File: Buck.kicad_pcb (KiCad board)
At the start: 2 copper layers, 33.5 x 40.3 mm, 15 parts, among them J1 IN, J2 OUT, J3 Measure, U1 LT1936

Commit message: small tweaks trace layout
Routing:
- net Net-(D3-K): track 2.69 -> 4.24 mm
- net VCC: track 11.2 -> 9.96 mm
- net Id: track 36.9 -> 36.3 mm
- net Net-(R2-Pad2): track 5.30 -> 5.85 mm
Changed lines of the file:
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@@
 		(tags "capacitor handsolder")
 		(property "Reference" "C2"
-			(at 0 -1.85 0)
+			(at -3.55 -0.05 0)
 			(layer "F.SilkS")
 			(effects
@@
 		)
 	)
-	(via
-		(at 96.6 79.8)
-		(size 0.6)
-		(drill 0.3)
-		(layers "F.Cu" "B.Cu")
-		(free yes)
+	(segment
+		(start 97.7 79.8)
+		(end 98.075 79.8)
+		(width 0.25)
+		(layer "F.Cu")
 		(net 1)
 	)
+	(segment
+		(start 97.1 79.1)
+		(end 97.1 79.2)
+		(width 0.25)
+		(layer "F.Cu")
+		(net 1)
+	)
+	(segment
+		(start 97.1 79.2)
+		(end 97.7 79.8)
+		(width 0.25)
+		(layer "F.Cu")
+		(net 1)
+	)
+	(segment
+		(start 98.075 79.8)
+		(end 98.09 79.815)
+		(width 0.25)
+		(layer "F.Cu")
+		(net 1)
+	)
+	(via
+		(at 97.1 79.1)
+		(size 0.6)
+		(drill 0.3)
+		(layers "F.Cu" "B.Cu")
+		(free yes)
+		(net 1)
+	)
 	(via
 		(at 94.2 79.1)
@@
 	)
 	(segment
-		(start 94.2 79.1)
-		(end 94.9 79.8)
+		(start 97.1 79.1)
+		(end 94.2 79.1)
 		(width 0.5)
 		(layer "B.Cu")
 		(net 1)
 	)
-	(segment
-		(start 94.9 79.8)
-		(end 96.6 79.8)
-		(width 0.5)
-		(layer "B.Cu")
-		(net 1)
-	)
 	(via
 		(at 93.5 87.4)
@@
 		(net 3)
 	)
-	(via
-		(at 96.1 78.1)
-		(size 0.6)
-		(drill 0.3)
-		(layers "F.Cu" "B.Cu")
+	(segment
+		(start 103.365 81.765)
+		(end 102.39 81.765)
+		(width 0.35)
+		(layer "F.Cu")
 		(net 4)
 	)
-	(via
-		(at 103.7 82.1)
-		(size 0.6)
-		(drill 0.3)
-		(layers "F.Cu" "B.Cu")
-		(free yes)
+	(segment
+		(start 103.7 81.8)
+		(end 103.4 81.8)
+		(width 0.35)
+		(layer "F.Cu")
 		(net 4)
 	)
 	(segment
-		(start 103.7 82.1)
+		(start 103.4 81.8)
+		(end 103.365 81.765)
+		(width 0.35)
+		(layer "F.Cu")
+		(net 4)
+	)
+	(via
+		(at 98.7 77.6)
+		(size 0.6)
+		(drill 0.3)
+		(layers "F.Cu" "B.Cu")
+		(net 4)
+	)
+	(via
+		(at 103.7 81.8)
+		(size 0.6)
+		(drill 0.3)
+		(layers "F.Cu" "B.Cu")
+		(free yes)
+		(net 4)
+	)
+	(segment
+		(start 102.5 77.5)
 		(end 103.7 78.7)
 		(width 0.5)
@@
 	)
 	(segment
-		(start 103.1 78.1)
-		(end 96.1 78.1)
+		(start 103.7 78.7)
+		(end 103.7 81.8)
 		(width 0.5)
 		(layer "B.Cu")
@@
 	)
 	(segment
-		(start 103.7 78.7)
-		(end 103.1 78.1)
+		(start 98.8 77.5)
+		(end 102.5 77.5)
 		(width 0.5)
 		(layer "B.Cu")
@@
 	)
 	(segment
-		(start 92.8 104.9)
-		(end 103.1 104.9)
+		(start 98.7 77.6)
+		(end 98.8 77.5)
+		(width 0.5)
+		(layer "B.Cu")
+		(net 4)
+	)
+	(segment
+		(start 91.33 103.73)
+		(end 92.5 104.9)
 		(width 0.5)
 		(layer "B.Cu")
@@
 	)
 	(segment
+		(start 92.5 104.9)
+		(end 103.1 104.9)
+		(width 0.5)
+		(layer "B.Cu")
+		(net 5)
+	)
+	(segment
+		(start 104.5 103.5)
+		(end 104.5 101.2825)
+		(width 0.5)
+		(layer "B.Cu")
+		(net 5)
+	)
+	(segment
+		(start 91.33 103.25)
+		(end 91.33 103.73)
+		(width 0.5)
+		(layer "B.Cu")
+		(net 5)
+	)
+	(segment
 		(start 103.1 104.9)
 		(end 104.5 103.5)
-		(width 0.5)
-		(layer "B.Cu")
-		(net 5)
-	)
-	(segment
-		(start 104.5 103.5)
-		(end 104.5 101.2825)
-		(width 0.5)
-		(layer "B.Cu")
-		(net 5)
-	)
-	(segment
-		(start 91.33 103.25)
-		(end 91.33 103.43)
-		(width 0.5)
-		(layer "B.Cu")
-		(net 5)
-	)
-	(segment
-		(start 91.33 103.43)
-		(end 92.8 104.9)
 		(width 0.5)
 		(layer "B.Cu")
@@
 	)
 	(segment
-		(start 108.35 91.75)
-		(end 109.1 91.75)
-		(width 0.25)
-		(layer "F.Cu")
-		(net 7)
-	)
-	(segment
-		(start 107.4 90.8)
-		(end 108.35 91.75)
+		(start 106.95 90.8)
+		(end 109.1 90.8)
 		(width 0.25)
 		(layer "F.Cu")
@@
 	)
 	(segment
-		(start 106.95 90.8)
-		(end 107.4 90.8)
+		(start 109.1 90.8)
+		(end 109.1 91.75)
 		(width 0.25)
 		(layer "F.Cu")
@@
 	)
 	(segment
+		(start 101.8 87.8)
+		(end 103.5 86.1)
+		(width 0.5)
+		(layer "F.Cu")
+		(net 9)
+	)
+	(segment
 		(start 105.4 86.8)
 		(end 106.4 87.8)
@@
 	)
 	(segment
-		(start 104.5 86.8)
+		(start 102.9 87.3)
+		(end 102.9 86)
+		(width 0.5)
+		(layer "F.Cu")
+		(net 9)
+	)
+	(segment
+		(start 103.5 86.1)
+		(end 104.2 86.8)
+		(width 0.5)
+		(layer "F.Cu")
+		(net 9)
+	)
+	(segment
+		(start 104.2 86.8)
 		(end 105.4 86.8)
 		(width 0.5)
@@
 		(net 9)
 	)
-	(segment
-		(start 103.7 86.8)
-		(end 102.9 86)
-		(width 0.5)
-		(layer "F.Cu")
+	(via
+		(at 101.8 87.8)
+		(size 0.6)
+		(drill 0.3)
+		(layers "F.Cu" "B.Cu")
 		(net 9)
 	)
 	(segment
-		(start 104.5 86.8)
-		(end 103.7 86.8)
-		(width 0.5)
-		(layer "F.Cu")
-		(net 9)
-	)
-	(via
-		(at 104.5 86.8)
-		(size 0.6)
-		(drill 0.3)
-		(layers "F.Cu" "B.Cu")
-		(net 9)
-	)
-	(segment
-		(start 96.4 86.8)
-		(end 95.2 85.6)
+		(start 101.7 87.7)
+		(end 95.8 87.7)
 		(width 0.5)
 		(layer "B.Cu")
@@
 	)
 	(segment
-		(start 90.8 85.6)
-		(end 88.79 87.61)
+		(start 95.8 87.7)
+		(end 94.4 86.3)
 		(width 0.5)
 		(layer "B.Cu")
@@
 	)
 	(segment
-		(start 95.2 85.6)
-		(end 90.8 85.6)
+		(start 94.4 86.3)
+		(end 91.5 86.3)
 		(width 0.5)
 		(layer "B.Cu")
@@
 	)
 	(segment
-		(start 88.79 87.61)
+		(start 88.79 89.01)
 		(end 88.79 103.25)
 		(width 0.5)
@@
 	)
 	(segment
-		(start 104.5 86.8)
-		(end 96.4 86.8)
+		(start 101.8 87.8)
+		(end 101.7 87.7)
+		(width 0.5)
+		(layer "B.Cu")
+		(net 9)
+	)
+	(segment
+		(start 91.5 86.3)
+		(end 88.79 89.01)
 		(width 0.5)
 		(layer "B.Cu")
@@
 		(polygon
 			(pts
-				(xy 90.5 79.75) (xy 87.75 79.75) (xy 87.75 85.75) (xy 92.25 85.75) (xy 92.25 89.05) (xy 98.05 89.05)
-				(xy 98.05 92.8) (xy 103 92.8) (xy 103 89.6) (xy 104.9 89.6) (xy 104.9 94.761907) (xy 106.039783 94.760217)
-				(xy 106 102.7) (xy 102.8 102.7) (xy 101.428837 99.357791) (xy 85.25 96.3) (xy 85.25 76.25) (xy 90.5 76.25)
+				(xy 90.5 79.75) (xy 87.75 79.75) (xy 87.75 85.75) (xy 92.25 85.75) (xy 92.25 89.05) (xy 98.25 89.05)
+				(xy 98.25 92.8) (xy 103 92.8) (xy 103 90.1) (xy 105.3 90.1) (xy 105.3 94.761313) (xy 107.439797 94.758142)
+				(xy 107.400003 102.7) (xy 102.8 102.7) (xy 100.018703 95.920591) (xy 85.25 93.129314) (xy 85.25 76.25)
+				(xy 90.5 76.25)
 			)
 		)
@@
 	)
 	(zone
-		(net 4)
-		(net_name "VCC")
-		(layer "F.Cu")
-		(hatch edge 0.5)
-		(priority 100)
-		(connect_pads
-			(clearance 0.25)
-		)
-		(min_thickness 0.25)
-		(filled_areas_thickness no)
-		(fill yes
-			(thermal_gap 0.5)
-			(thermal_bridge_width 0.5)
-		)
-		(polygon
-			(pts
-				(xy 101.7 81.5) (xy 104.3 81.5) (xy 104.3 82.4) (xy 101.7 82.4)
-			)
-		)
-	)
-	(zone
 		(net 3)
 		(net_name "GND")
@@
 		(filled_areas_thickness no)
 		(fill yes
-			(thermal_gap 0.5)
+			(thermal_gap 0.25)
 			(thermal_bridge_width 0.5)
 		)
 		(polygon
 			(pts
-				(xy 100.3 69.25) (xy 100.25 76.25) (xy 100.25 77.5) (xy 97 77.5) (xy 97 79.4) (xy 96.3 79.4) (xy 96.3 80.3)
-				(xy 97.5 80.3) (xy 97.494384 80.694384) (xy 97 80.7) (xy 94.6 80.7) (xy 94.6 80) (xy 94.6 67.25)
-				(xy 100.3 67.25)
+				(xy 100.3 69.25) (xy 100.24795 76.589031) (xy 99.376469 78) (xy 97 78) (xy 97 79.4) (xy 97 79.4)
+				(xy 97 79.773828) (xy 97.5 80.3) (xy 97.494384 80.694384) (xy 97 80.7) (xy 94.6 80.7) (xy 94.6 80)
+				(xy 94.6 67.25) (xy 100.3 67.25)
 			)
 		)
@@
 			)
 		)
-	)
-	(zone
-		(net 1)
-		(net_name "Net-(D3-K)")
-		(layer "F.Cu")
-		(hatch edge 0.5)
-		(priority 4)
-		(connect_pads
-			(clearance 0.25)
-		)
-		(min_thickness 0.25)
-		(filled_areas_thickness no)
-		(fill yes
-			(thermal_gap 0.5)
-			(thermal_bridge_width 0.5)
-		)
-		(polygon
-			(pts
-				(xy 96.4 79.5) (xy 98.8 79.5) (xy 98.8 80.1) (xy 96.4 80.1)
-			)
-		)

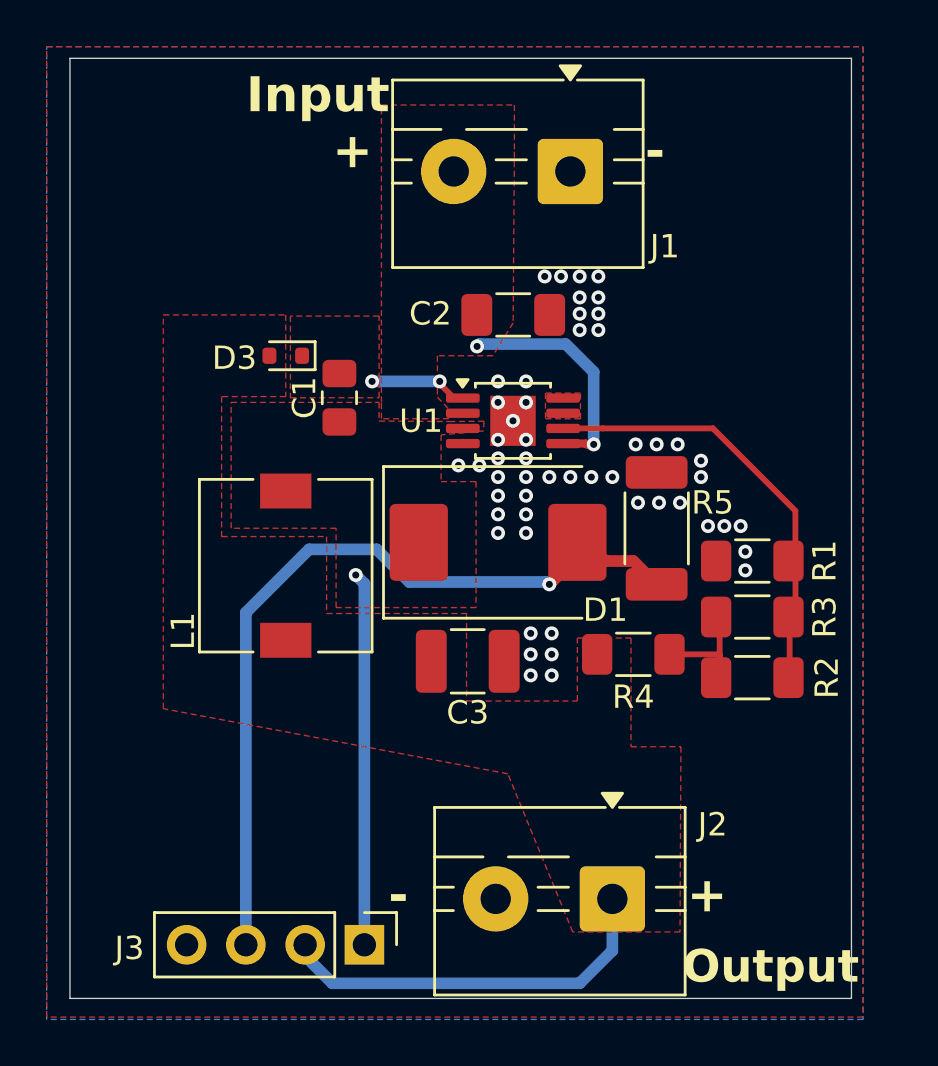
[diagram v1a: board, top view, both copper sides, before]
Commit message: addes extra silkscreen for info
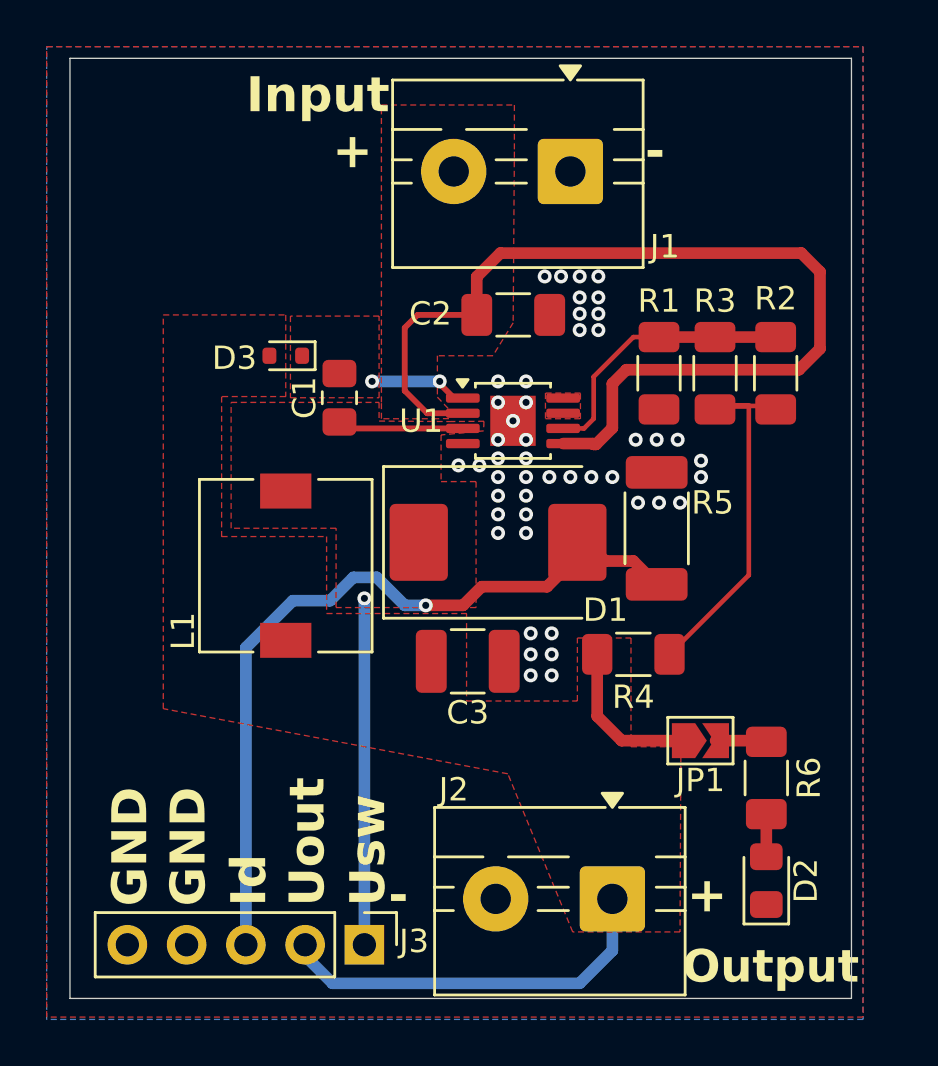
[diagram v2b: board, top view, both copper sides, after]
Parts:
- added D2: LED, LED_SMD:LED_0805_2012Metric_Pad1.15x1.40mm_HandSolder, F.Cu at (111.1, 100.5)
- added JP1: SolderJumper_2_Open, Jumper:SolderJumper-2_P1.3mm_Open_TrianglePad1.0x1.5mm, F.Cu at (108.3, 94.5)
- added R6: 1K, Resistor_SMD:R_1206_3216Metric_Pad1.30x1.75mm_HandSolder, F.Cu at (111.1, 96.1)
- C1: value 0.22uF -> 0.22uF 50V
- C2: value 10U 50V -> 10u 50V
- C3: value 47U 6,3V -> 47u 6,3V
- J3: footprint Connector_PinHeader_2.54mm:PinHeader_1x04_P2.54mm_Vertical -> Connector_PinHeader_2.54mm:PinHeader_1x05_P2.54mm_Vertical
- moved R2 13.1 mm to (111.5, 78.8), turned to -90 degrees
- moved R3 10.6 mm to (108.9, 78.8), turned to -90 degrees
- moved R1 8.99 mm to (106.5, 78.8), turned to -90 degrees
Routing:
- net VCC: track 9.96 -> 43.1 mm, vias 2 -> 0
- net Net-(R2-Pad2): track 5.85 -> 14.2 mm
- net Uout: track 16.9 -> 23.6 mm
- net Net-(U1-FB): track 18.5 -> 12.2 mm
- net Usw: track 16.0 -> 20.3 mm
- net Net-(JP1-B): track 0.00 -> 2.20 mm
- net Net-(D2-A): track 0.00 -> 1.82 mm
- net Id: track 36.3 -> 35.2 mm
- net GND: vias 52 -> 47
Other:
- board text added: "7V to 36V IN 3.3V OUT 1A"
- board text added: "GND"
- board text added: "Id"
- board text added: "Uout"
- board text added: "Usw"

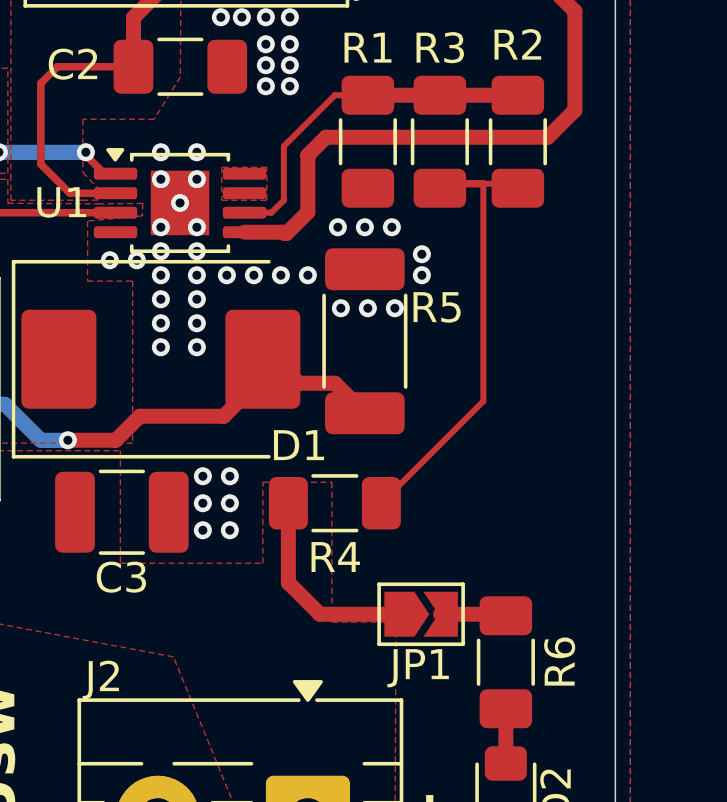
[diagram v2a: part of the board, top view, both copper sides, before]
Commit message: solder pad tweak
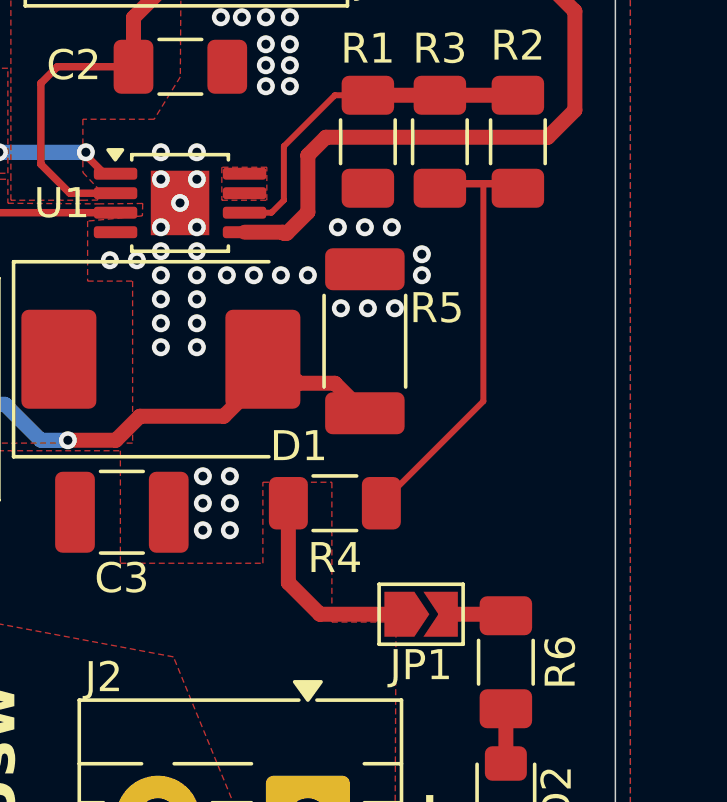
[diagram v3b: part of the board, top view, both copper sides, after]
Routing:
- net Net-(R2-Pad2): track 14.2 -> 15.2 mm
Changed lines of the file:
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@@
 	)
 	(segment
-		(start 106.95 90.8)
+		(start 109.4 80.15)
+		(end 111.35 80.15)
+		(width 0.25)
+		(layer "F.Cu")
+		(net 7)
+	)
+	(segment
+		(start 110.35 80.15)
 		(end 110.35 87.4)
 		(width 0.2)
@@
 	)
 	(segment
-		(start 110.35 80.15)
-		(end 111.35 80.15)
+		(start 111.35 80.15)
+		(end 111.5 80.3)
+		(width 0.25)
+		(layer "F.Cu")
+		(net 7)
+	)
+	(segment
+		(start 111.35 80.15)
+		(end 110.35 80.15)
 		(width 0.2)
 		(layer "F.Cu")
@@
 	(segment
 		(start 110.35 87.4)
-		(end 110.35 80.15)
-		(width 0.2)
-		(layer "F.Cu")
-		(net 7)
-	)
-	(segment
-		(start 109.4 80.15)
-		(end 110.35 80.15)
-		(width 0.25)
-		(layer "F.Cu")
-		(net 7)
-	)
-	(segment
-		(start 111.35 80.15)
-		(end 111.5 80.3)
+		(end 106.95 90.8)
 		(width 0.2)
 		(layer "F.Cu")
@@
 	)
 	(segment
-		(start 108.925 94.5)
+		(start 109.3 94.5)
 		(end 111.05 94.5)
 		(width 0.5)
